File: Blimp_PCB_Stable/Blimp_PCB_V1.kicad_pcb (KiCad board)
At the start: 2 copper layers, 109.9 x 62 mm, 25 parts, among them J1 S8B-PH-K-S, J2 S4B-XH-A

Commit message: Fixed all the problems
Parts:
- B1: footprint JST Connector:XT30 -> XT30:XT30
- P8: footprint Blimp Library:Orange_Pi_5B -> Orange_Pi_5B:Orange_Pi_5B
- P9: footprint TerminalBlock_Phoenix:TerminalBlock_Phoenix_MKDS-1,5-2_1x02_P5.00mm_Horizontal -> TerminalBlock:TerminalBlock_Phoenix_MKDS-1,5-2_1x02_P5.00mm_Horizontal
- U3: footprint Connector_JST:JST_XH_S2B-XH-A_1x02_P2.50mm_Horizontal -> JST Connector:JST_XH_S2B-XH-A_1x02_P2.50mm_Horizontal
- moved J2 1.00 mm to (178.6, 132.9)
- moved P4 1.00 mm to (159.0, 127.2)
- moved P5 1.00 mm to (197.2, 127.2)
- moved U3 1.00 mm to (137.5, 127.2)
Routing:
- net Net-(P5-Pad1): track 15.8 -> 12.5 mm
- net +5V: track 103.4 -> 102.3 mm
- net Net-(P8-TXD.0): track 62.3 -> 61.3 mm
- net Net-(P8-SDA.5): track 91.1 -> 90.1 mm
- net Net-(P8-RXD.0): track 69.8 -> 69.1 mm
- net Net-(P4-PWM): track 74.9 -> 74.1 mm
- net GND: track 22.0 -> 21.4 mm, vias 4 -> 3
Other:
- board text removed: "${REFERENCE}"

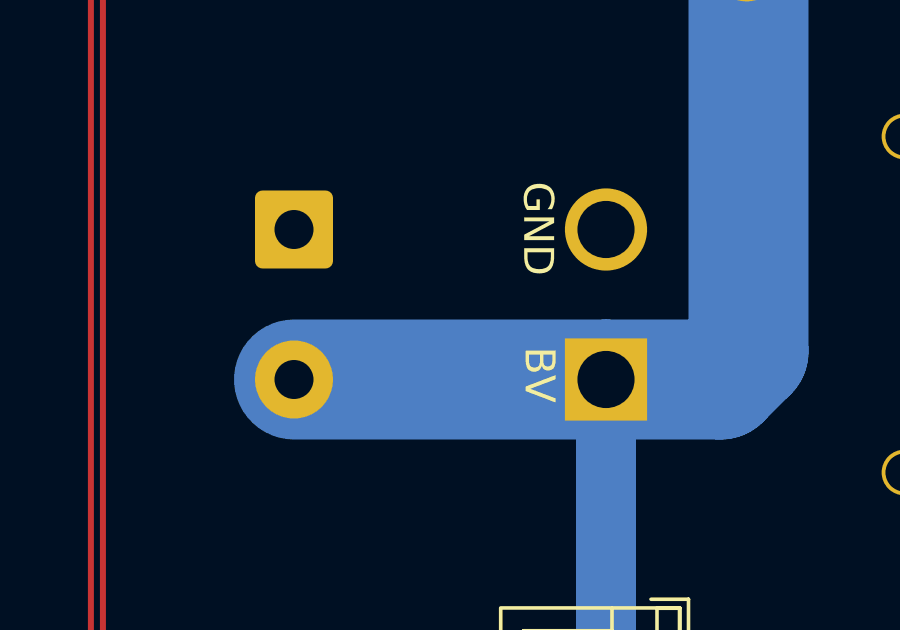
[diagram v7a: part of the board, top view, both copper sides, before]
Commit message: fixed DRC and footprint library erros
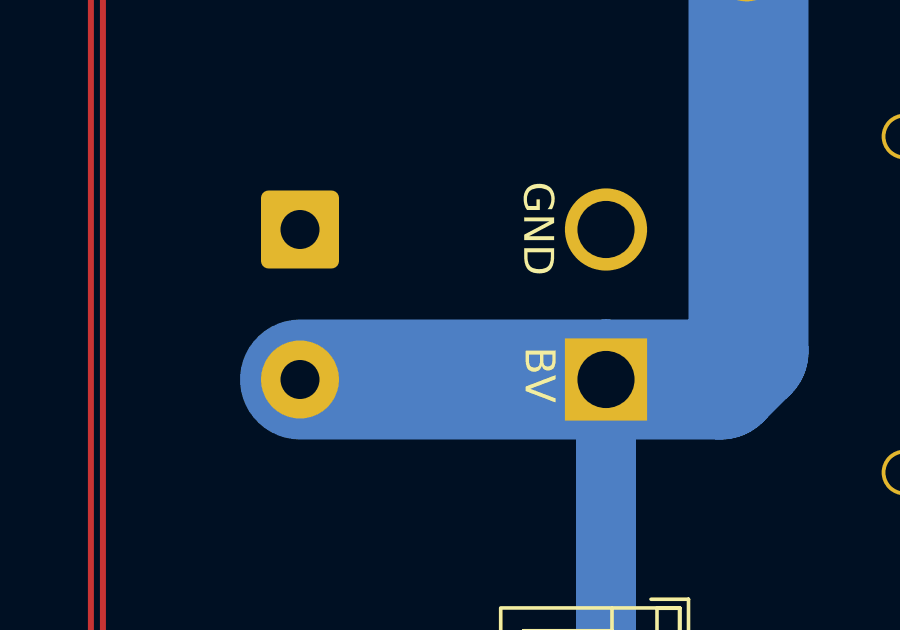
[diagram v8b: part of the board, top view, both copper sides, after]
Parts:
- P9: footprint TerminalBlock:TerminalBlock_Phoenix_MKDS-1,5-2_1x02_P5.00mm_Horizontal -> TerminalBlock_Phoenix:TerminalBlock_Phoenix_MKDS-1,5-2_1x02_P5.00mm_Horizontal
- moved P9 2.51 mm to (190.5, 97.4)
